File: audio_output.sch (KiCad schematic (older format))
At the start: 21 parts, among them U8 OPA1664

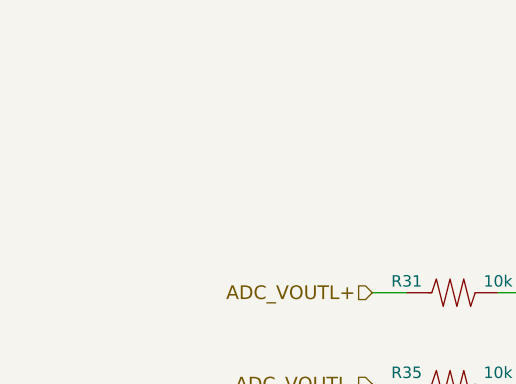
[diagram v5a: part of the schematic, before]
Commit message: Fixed decoupling cap polarity on output op-amp, added bias to analog input, changed capacitor footprints to reflect new capacitor selections
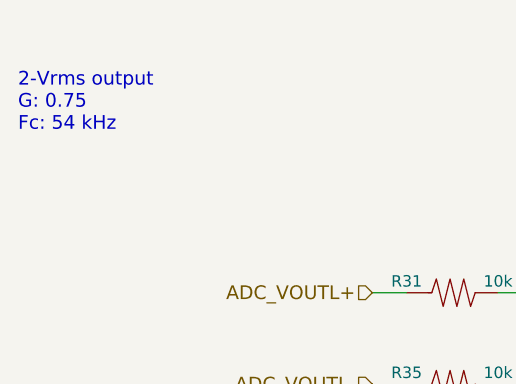
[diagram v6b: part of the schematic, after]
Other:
- note added: "2-Vrms output\nG: 0.75\nFc: 54 kHz"
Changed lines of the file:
@@
 	5150 1500 5150 1650
 $Comp
-L -5V #PWR97
+L -5V #PWR097
 U 1 1 5A4A0210
 P 6500 1500
-F 0 "#PWR97" H 6500 1640 20  0001 C CNN
+F 0 "#PWR097" H 6500 1640 20  0001 C CNN
 F 1 "-5V" H 6500 1610 30  0000 C CNN
 F 2 "" H 6500 1500 60  0000 C CNN
@@
 $EndComp
 $Comp
-L +5V #PWR98
+L +5V #PWR098
 U 1 1 5A4A0216
 P 6500 2650
-F 0 "#PWR98" H 6500 2740 20  0001 C CNN
+F 0 "#PWR098" H 6500 2740 20  0001 C CNN
 F 1 "+5V" H 6500 2740 30  0000 C CNN
 F 2 "" H 6500 2650 60  0000 C CNN
@@
 $EndComp
 $Comp
-L GND #PWR100
+L GND #PWR099
 U 1 1 5A4A0477
 P 4700 3400
-F 0 "#PWR100" H 4700 3400 30  0001 C CNN
+F 0 "#PWR099" H 4700 3400 30  0001 C CNN
 F 1 "GND" H 4700 3330 30  0001 C CNN
 F 2 "" H 4700 3400 60  0000 C CNN
@@
 Connection ~ 4000 2350
 $Comp
-L GND #PWR99
+L GND #PWR0100
 U 1 1 5A4A0BAE
 P 4000 3400
-F 0 "#PWR99" H 4000 3400 30  0001 C CNN
+F 0 "#PWR0100" H 4000 3400 30  0001 C CNN
 F 1 "GND" H 4000 3330 30  0001 C CNN
 F 2 "" H 4000 3400 60  0000 C CNN
@@
 	5200 4450 5200 4600
 $Comp
-L -5V #PWR101
+L -5V #PWR0101
 U 1 1 5A4A1169
 P 6550 4450
-F 0 "#PWR101" H 6550 4590 20  0001 C CNN
+F 0 "#PWR0101" H 6550 4590 20  0001 C CNN
 F 1 "-5V" H 6550 4560 30  0000 C CNN
 F 2 "" H 6550 4450 60  0000 C CNN
@@
 $EndComp
 $Comp
-L +5V #PWR102
+L +5V #PWR0102
 U 1 1 5A4A116F
 P 6550 5600
-F 0 "#PWR102" H 6550 5690 20  0001 C CNN
+F 0 "#PWR0102" H 6550 5690 20  0001 C CNN
 F 1 "+5V" H 6550 5690 30  0000 C CNN
 F 2 "" H 6550 5600 60  0000 C CNN
@@
 $EndComp
 $Comp
-L GND #PWR104
+L GND #PWR0103
 U 1 1 5A4A11CB
 P 4750 6350
-F 0 "#PWR104" H 4750 6350 30  0001 C CNN
+F 0 "#PWR0103" H 4750 6350 30  0001 C CNN
 F 1 "GND" H 4750 6280 30  0001 C CNN
 F 2 "" H 4750 6350 60  0000 C CNN
@@
 Connection ~ 4050 5300
 $Comp
-L GND #PWR103
+L GND #PWR0104
 U 1 1 5A4A1201
 P 4050 6350
-F 0 "#PWR103" H 4050 6350 30  0001 C CNN
+F 0 "#PWR0104" H 4050 6350 30  0001 C CNN
 F 1 "GND" H 4050 6280 30  0001 C CNN
 F 2 "" H 4050 6350 60  0000 C CNN
@@
 Wire Wire Line
 	5150 2450 5150 2650
+Text Notes 1000 1250 0    60   ~ 0
+2-Vrms output\nG: 0.75\nFc: 54 kHz
 $EndSCHEMATC

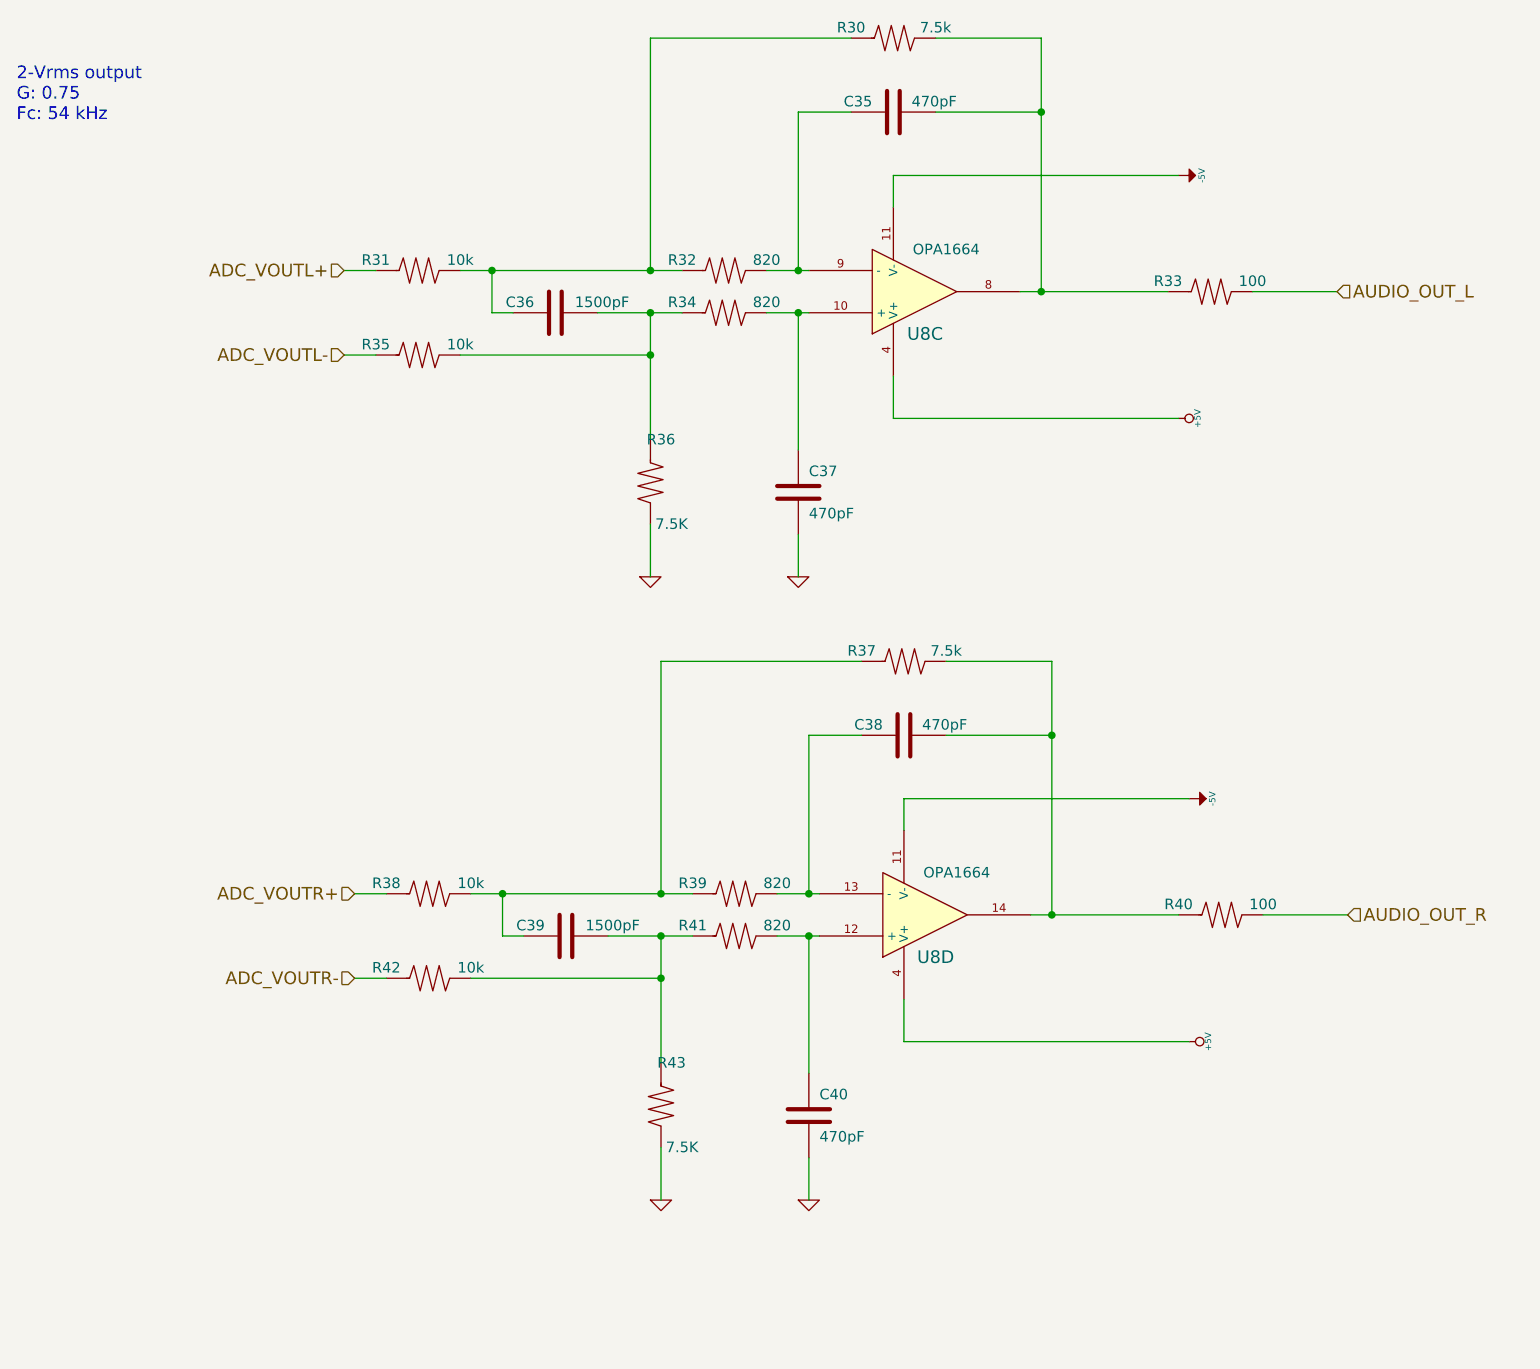
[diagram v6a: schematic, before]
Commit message: Updated audio capacitor types to reflect BOM
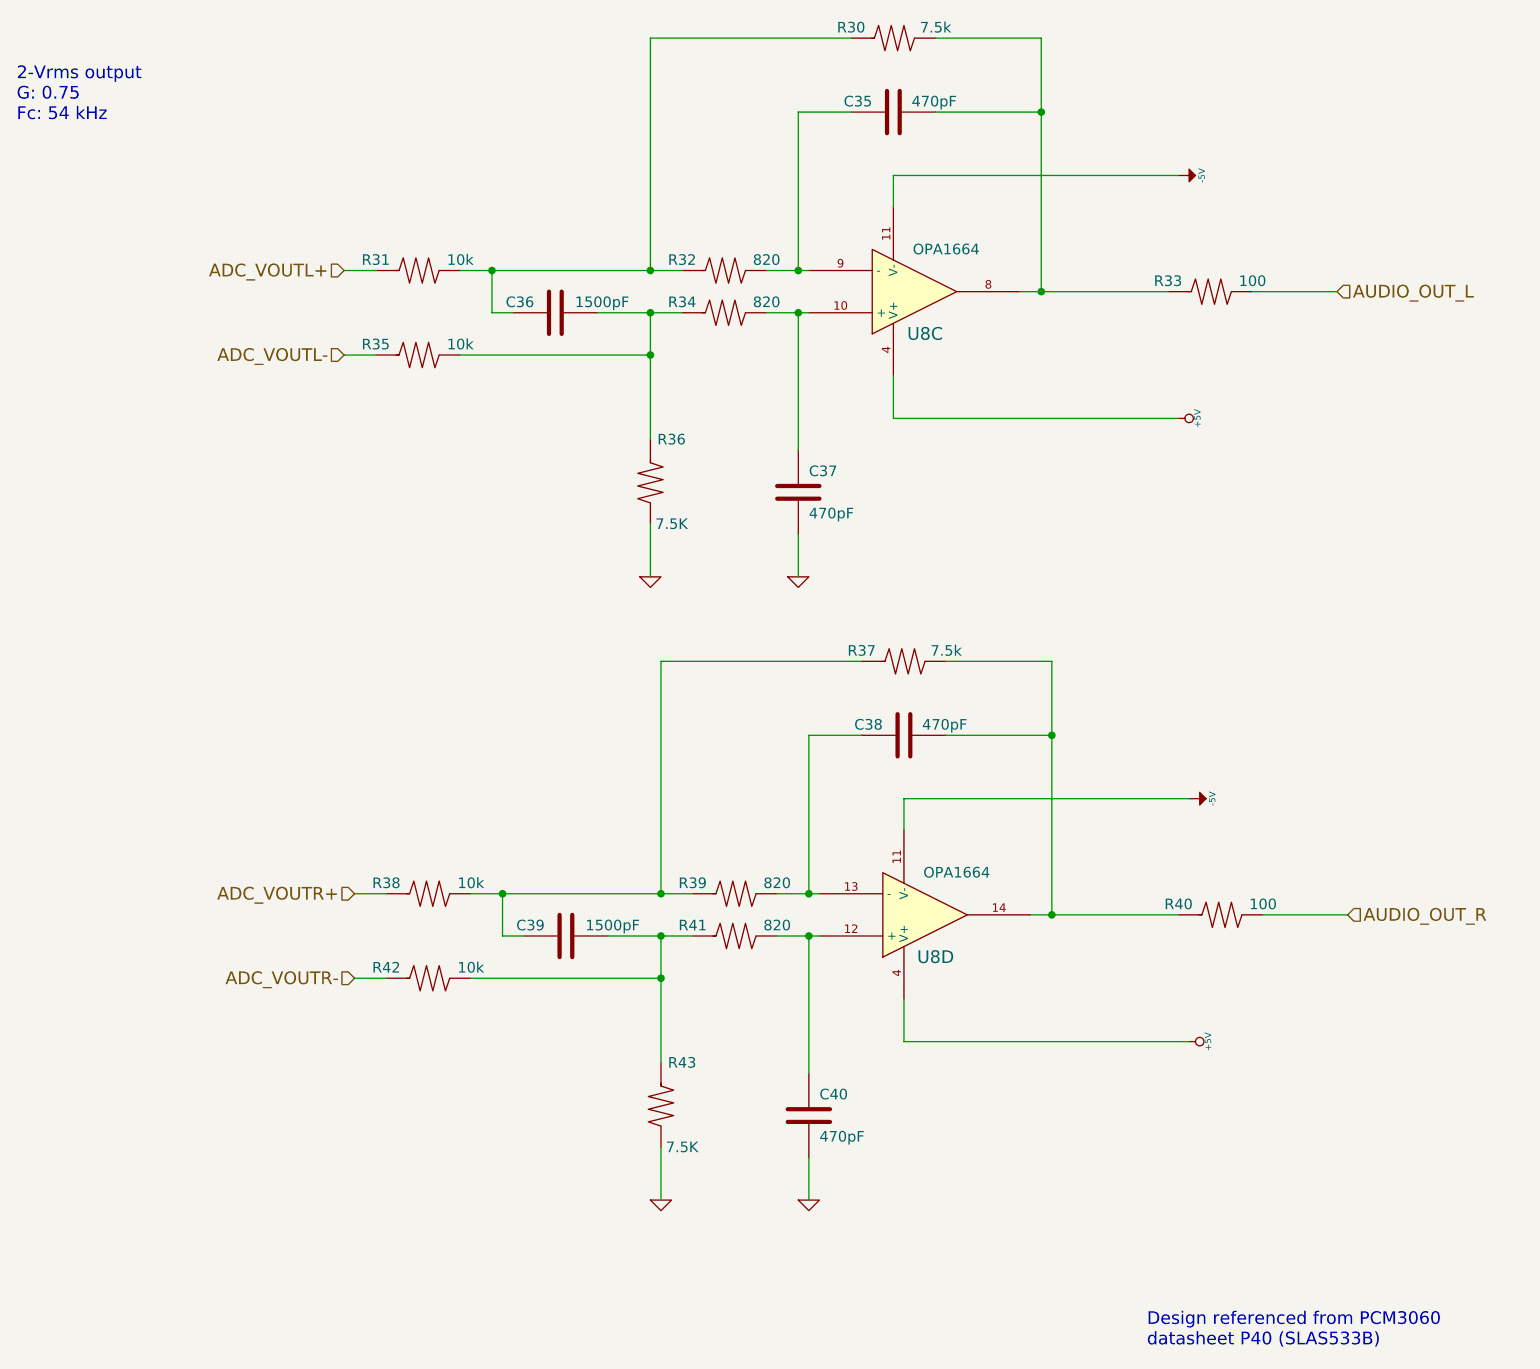
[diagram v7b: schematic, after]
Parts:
- C35, C36, C37, C38, C39, C40: footprint (none) -> muse-v3:C_Rect_L7.2_W4.5_P5
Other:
- note added: "Design referenced from PCM3060\ndatasheet P40 (SLAS533B)"
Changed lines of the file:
@@
 F 0 "C35" V 5200 1300 50  0000 L CNN
 F 1 "470pF" V 5200 900 50  0000 L CNN
-F 2 "" H 5150 1200 60  0001 C CNN
+F 2 "muse-v3:C_Rect_L7.2_W4.5_P5" H 5150 1200 60  0001 C CNN
 F 3 "" H 5150 1200 60  0000 C CNN
 	1    5150 1200
@@
 F 0 "C37" H 4750 3100 50  0000 L CNN
 F 1 "470pF" H 4750 2900 50  0000 L CNN
-F 2 "" H 4700 3000 60  0001 C CNN
+F 2 "muse-v3:C_Rect_L7.2_W4.5_P5" H 4700 3000 60  0001 C CNN
 F 3 "" H 4700 3000 60  0000 C CNN
 	1    4700 3000
@@
 F 0 "C36" V 3600 2250 50  0000 L CNN
 F 1 "1500pF" V 3600 1800 50  0000 L CNN
-F 2 "" H 3550 2150 60  0001 C CNN
+F 2 "muse-v3:C_Rect_L7.2_W4.5_P5" H 3550 2150 60  0001 C CNN
 F 3 "" H 3550 2150 60  0000 C CNN
 	1    3550 2150
@@
 U 1 1 5A4A0B17
 P 4000 2950
-F 0 "R36" V 3800 3000 50  0000 C CNN
+F 0 "R36" V 3800 3050 50  0000 C CNN
 F 1 "7.5K" V 4200 3050 50  0000 C CNN
 F 2 "" H 4000 2950 60  0001 C CNN
@@
 F 0 "C38" V 5250 4250 50  0000 L CNN
 F 1 "470pF" V 5250 3850 50  0000 L CNN
-F 2 "" H 5200 4150 60  0001 C CNN
+F 2 "muse-v3:C_Rect_L7.2_W4.5_P5" H 5200 4150 60  0001 C CNN
 F 3 "" H 5200 4150 60  0000 C CNN
 	1    5200 4150
@@
 F 0 "C40" H 4800 6050 50  0000 L CNN
 F 1 "470pF" H 4800 5850 50  0000 L CNN
-F 2 "" H 4750 5950 60  0001 C CNN
+F 2 "muse-v3:C_Rect_L7.2_W4.5_P5" H 4750 5950 60  0001 C CNN
 F 3 "" H 4750 5950 60  0000 C CNN
 	1    4750 5950
@@
 F 0 "C39" V 3650 5200 50  0000 L CNN
 F 1 "1500pF" V 3650 4750 50  0000 L CNN
-F 2 "" H 3600 5100 60  0001 C CNN
+F 2 "muse-v3:C_Rect_L7.2_W4.5_P5" H 3600 5100 60  0001 C CNN
 F 3 "" H 3600 5100 60  0000 C CNN
 	1    3600 5100
@@
 U 1 1 5A4A11F9
 P 4050 5900
-F 0 "R43" V 3850 5950 50  0000 C CNN
+F 0 "R43" V 3850 6000 50  0000 C CNN
 F 1 "7.5K" V 4250 6000 50  0000 C CNN
 F 2 "" H 4050 5900 60  0001 C CNN
@@
 Text Notes 1000 1250 0    60   ~ 0
 2-Vrms output\nG: 0.75\nFc: 54 kHz
+Text Notes 6350 7050 0    60   ~ 0
+Design referenced from PCM3060\ndatasheet P40 (SLAS533B)
 $EndSCHEMATC

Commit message: Added more footprint associations, added new footprints to lib
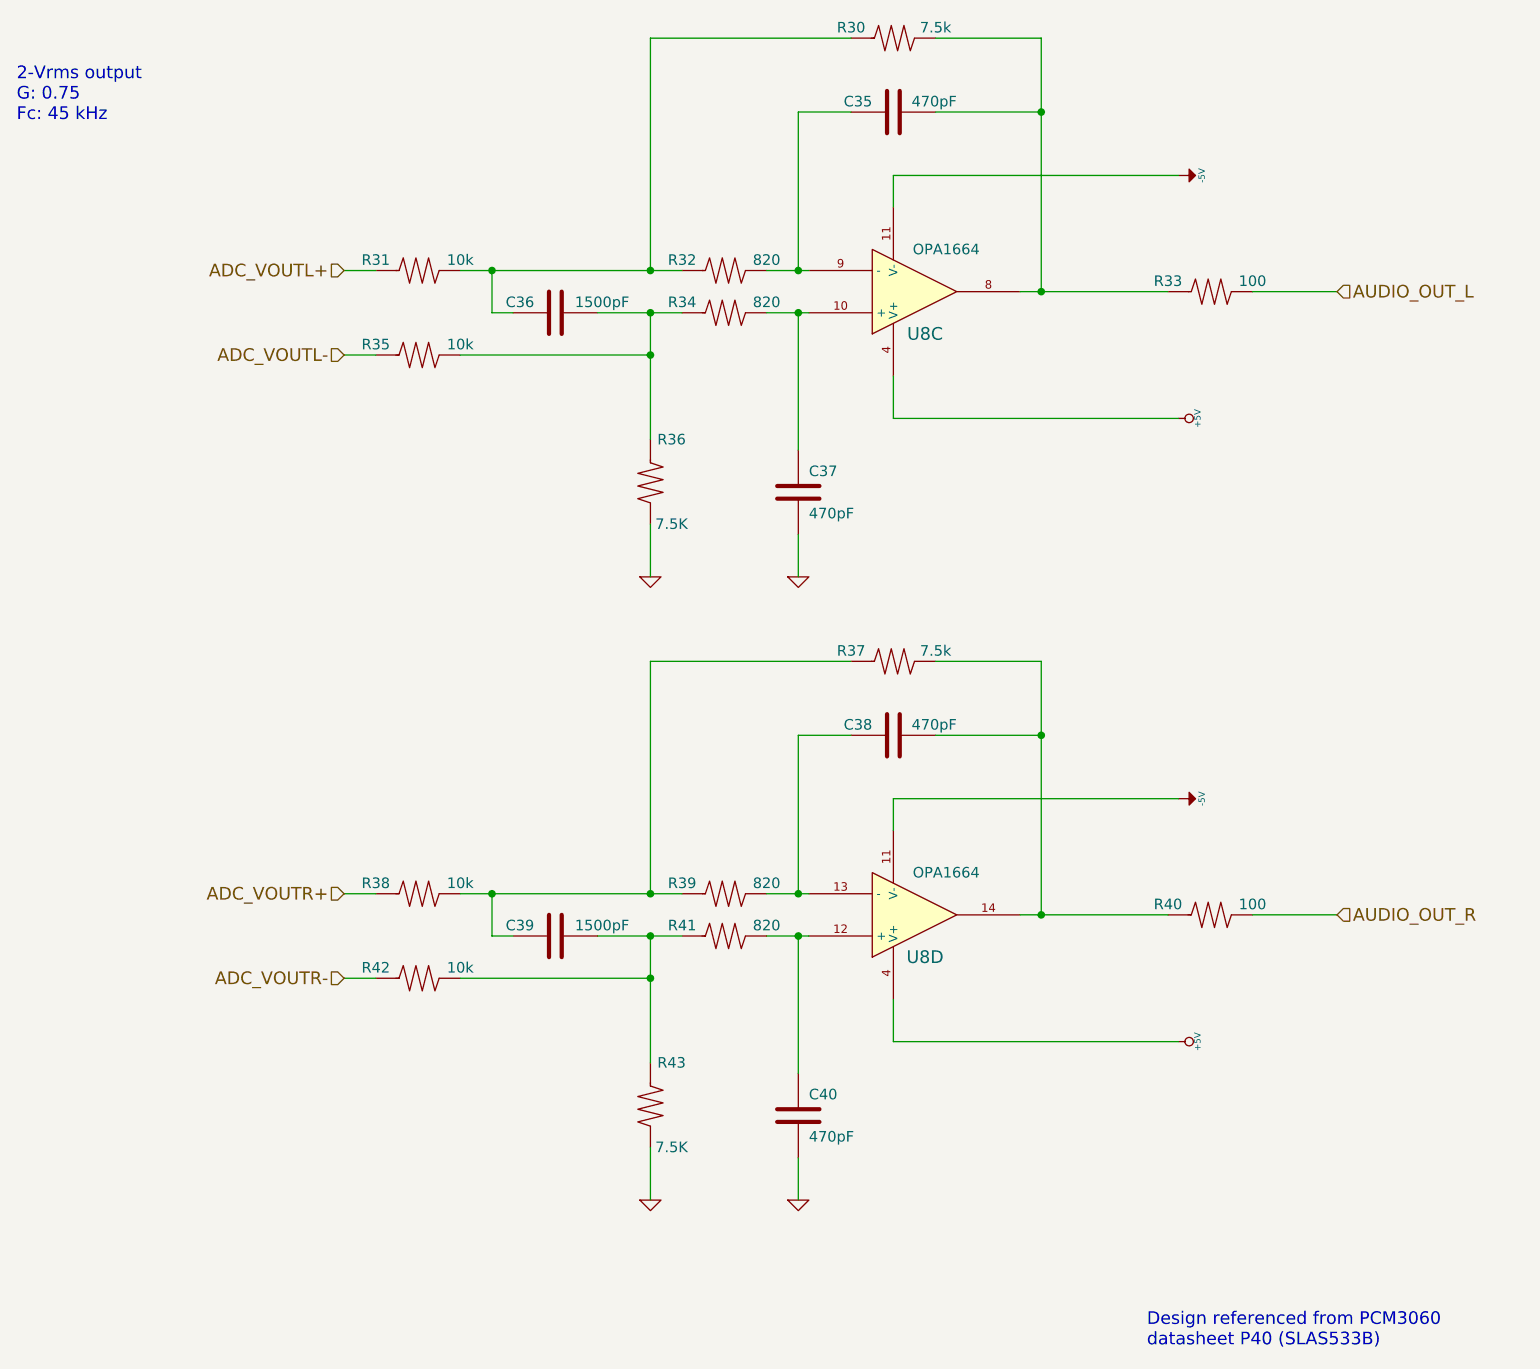
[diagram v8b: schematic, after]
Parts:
- R30, R31, R32, R33, R34, R35, R36, R37, R38, R39, R40, R41, R42, R43: footprint (none) -> Resistors_SMD:R_0805_HandSoldering
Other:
- note added: "2-Vrms output\nG: 0.75\nFc: 45 kHz"
- note removed: "2-Vrms output\nG: 0.75\nFc: 54 kHz"
- moved on the sheet: C38, C39, C40, R37, R38, R39, R40, R41, R42, R43, U8D
